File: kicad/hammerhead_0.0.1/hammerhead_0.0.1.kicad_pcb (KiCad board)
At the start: 4 copper layers, 66.2 x 29.5 mm, 111 parts, among them J1 BATTERY_CONN, J2 M1_CONN, J3 M2_CONN, J4 JTAG, J5 DEBUG, J6 MM_DB_CONN, U1 STM32F103C8T6, U2 25LC256-I_SN, U3 MAX14870ETC_T, U4 MAX14870ETC_T, U5 L6983CQTR, U6 RT9193-33GB, U7 L6983CQTR, U8 L6983CQTR, U9 BMI270, Y1 16 MHz

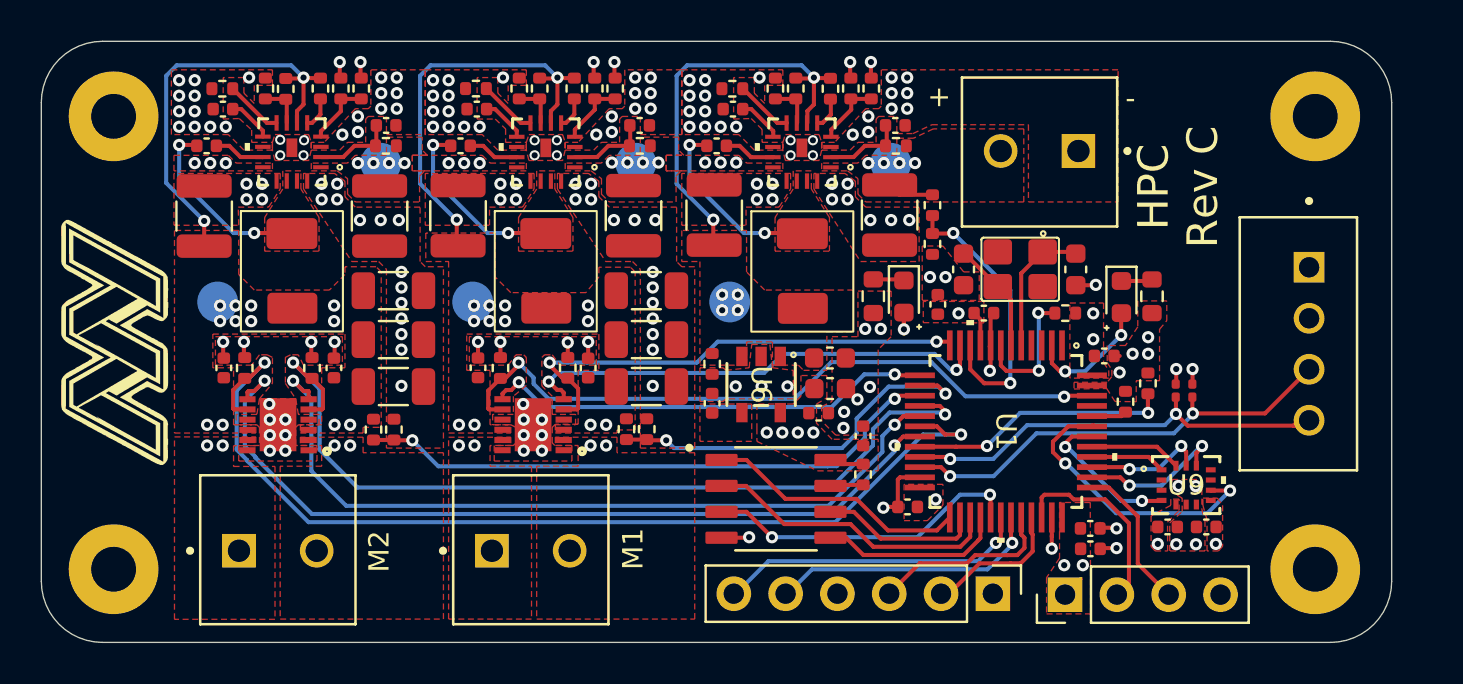
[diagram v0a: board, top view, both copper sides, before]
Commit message: replace i2c comms with can
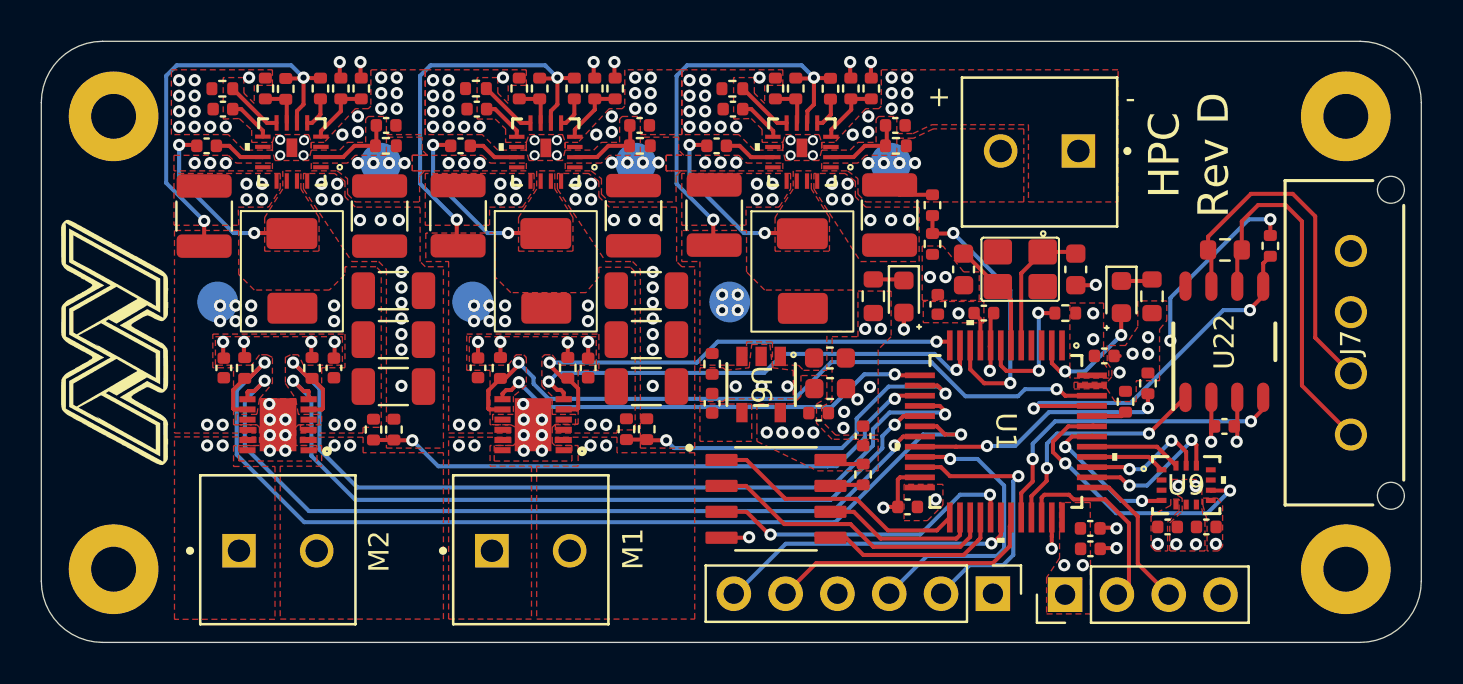
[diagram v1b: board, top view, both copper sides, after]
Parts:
- removed J6: MM_DB_CONN, B4B_XH_A:JST_B4B-XH-A
- removed R27, R28: 2k, 0201, Resistor_SMD:R_0201_0603Metric
- added C41: 0.1uF, Capacitor_SMD:C_0402_1005Metric, F.Cu at (175.8, 88.6)
- added J7: 436500427, 436500427:CONN_SD-43650-010_04_MOL, F.Cu at (182.1, 80.0)
- added R36: 10k, Resistor_SMD:R_0402_1005Metric, F.Cu at (178.1, 79.8)
- added R38: 120, Resistor_SMD:R_0603_1608Metric, F.Cu at (175.9, 80.0)
- added U22: TCAN337DR, TCAN337DR:D0008A_N, F.Cu at (175.8, 84.5)
- moved REF** 1.50 mm to (181.8, 73.4)
- moved REF** 1.50 mm to (181.8, 95.6)
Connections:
- U1 pad 21: I2C2_SCL -> INDIC_1
- U1 pad 22: I2C2_SDA -> INDIC_2
- U1 pad 32: INDIC_1 -> CAN_RX
- U1 pad 33: INDIC_2 -> CAN_TX
- U1 pad 45: unconnected-(U1A-PB8-Pad45) -> CAN_FAULT
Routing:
- net I2C2_SCL: track 23.1 -> 0.00 mm, vias 2 -> 0
- net I2C2_SDA: track 22.3 -> 0.00 mm, vias 2 -> 0
- net CAN_FAULT: track 0.00 -> 18.6 mm, vias 0 -> 2
- net /CAN_L: track 0.00 -> 18.3 mm
- net /CAN_H: track 0.00 -> 17.5 mm
- net CAN_RX: track 0.00 -> 16.4 mm, vias 0 -> 2
- net CAN_TX: track 0.00 -> 11.7 mm, vias 0 -> 2
- net 3V3B: track 8.59 -> 18.8 mm, vias 15 -> 16
- net INDIC_2: track 7.04 -> 13.7 mm, vias 0 -> 1
- net INDIC_1: track 9.12 -> 14.4 mm, vias 0 -> 1
- net GNDB: track 21.2 -> 23.4 mm, vias 170 -> 171
- net M2_DIR: track 39.0 -> 38.2 mm
- net UART1_RX: vias 1 -> 0
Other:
- board size 66.2 x 29.5 mm -> 67.6 x 29.5 mm
- board text added: "HPC Rev D"
- board text removed: "HPC Rev C"

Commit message: move thirdparty models to thirdparty dir
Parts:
- U2: footprint 25LC256-I/SN:SOIC127P599X175-8N -> 25LC256-I/SN:SOIC8-N_MC_MCH
- U3, U4: footprint MAX14870ETC_T:SON50P300X300X80-13N -> MAX14870ETC_T:21-0664B_MXM
